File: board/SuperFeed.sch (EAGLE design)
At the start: 16 parts

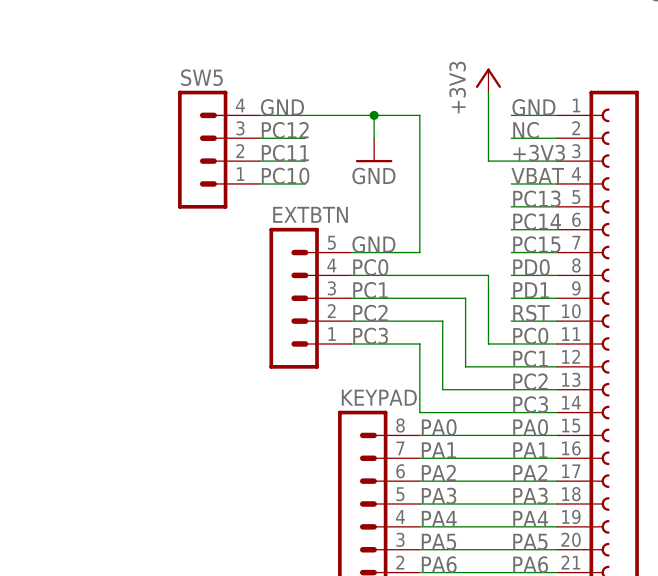
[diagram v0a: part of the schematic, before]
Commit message: Two more pins on extension connector
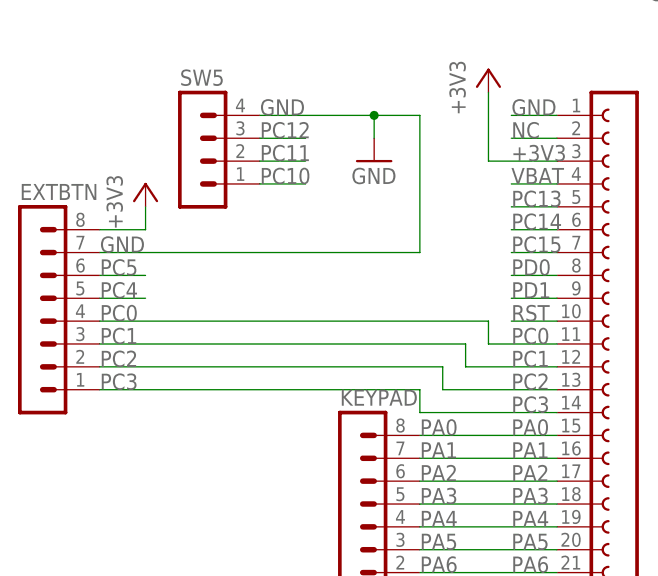
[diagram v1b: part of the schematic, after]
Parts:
- EXTBTN: device SuperFeed:MA05-1W -> SuperFeed:MA08-1W
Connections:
- net +3V3: now also EXTBTN.8
- net GND: now also EXTBTN.7; no longer EXTBTN.5
- net PC4: now also EXTBTN.5
- net PC5: now also EXTBTN.6
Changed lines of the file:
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@@
 <part name="R5" library="SuperFeed" deviceset="R-US_" device="0207/10" value="10k"/>
 <part name="P+5" library="SuperFeed" deviceset="+5V" device=""/>
-<part name="EXTBTN" library="SuperFeed" deviceset="MA05-1W" device=""/>
+<part name="EXTBTN" library="SuperFeed" deviceset="MA08-1W" device=""/>
+<part name="+3V3" library="SuperFeed" deviceset="+3V3" device=""/>
 </parts>
 <sheets>
@@
 <instance part="R5" gate="G$1" x="12.7" y="2.54"/>
 <instance part="P+5" gate="1" x="5.08" y="35.56"/>
-<instance part="EXTBTN" gate="G$1" x="12.7" y="76.2"/>
+<instance part="EXTBTN" gate="1" x="-15.24" y="73.66"/>
+<instance part="+3V3" gate="G$1" x="-2.54" y="88.9"/>
 </instances>
 <busses>
@@
 <wire x1="22.86" y1="96.52" x2="22.86" y2="93.98" width="0.1524" layer="91"/>
 <pinref part="GND5" gate="1" pin="GND"/>
-<pinref part="EXTBTN" gate="G$1" pin="5"/>
-<wire x1="20.32" y1="81.28" x2="27.94" y2="81.28" width="0.1524" layer="91"/>
-<wire x1="27.94" y1="81.28" x2="27.94" y2="96.52" width="0.1524" layer="91"/>
 <wire x1="27.94" y1="96.52" x2="22.86" y2="96.52" width="0.1524" layer="91"/>
 <junction x="22.86" y="96.52"/>
-<label x="20.32" y="81.28" size="1.778" layer="95"/>
+<pinref part="EXTBTN" gate="1" pin="7"/>
+<wire x1="-7.62" y1="81.28" x2="27.94" y2="81.28" width="0.1524" layer="91"/>
+<wire x1="27.94" y1="81.28" x2="27.94" y2="96.52" width="0.1524" layer="91"/>
+<label x="-7.62" y="81.28" size="1.778" layer="95"/>
 </segment>
 <segment>
@@
 <wire x1="96.52" y1="116.84" x2="88.9" y2="116.84" width="0.1524" layer="91"/>
 </segment>
+<segment>
+<pinref part="EXTBTN" gate="1" pin="8"/>
+<pinref part="+3V3" gate="G$1" pin="+3V3"/>
+<wire x1="-7.62" y1="83.82" x2="-2.54" y2="83.82" width="0.1524" layer="91"/>
+<wire x1="-2.54" y1="83.82" x2="-2.54" y2="86.36" width="0.1524" layer="91"/>
+</segment>
 </net>
 <net name="NC" class="0">
@@
 <segment>
 <pinref part="LEFT" gate="G$1" pin="23"/>
+<label x="38.1" y="40.64" size="1.778" layer="95"/>
 <wire x1="43.18" y1="40.64" x2="38.1" y2="40.64" width="0.1524" layer="91"/>
-<label x="38.1" y="40.64" size="1.778" layer="95"/>
+</segment>
+<segment>
+<pinref part="EXTBTN" gate="1" pin="5"/>
+<wire x1="-7.62" y1="76.2" x2="-2.54" y2="76.2" width="0.1524" layer="91"/>
+<label x="-7.62" y="76.2" size="1.778" layer="95"/>
 </segment>
 </net>
@@
 <segment>
 <pinref part="LEFT" gate="G$1" pin="24"/>
+<label x="38.1" y="38.1" size="1.778" layer="95"/>
 <wire x1="43.18" y1="38.1" x2="38.1" y2="38.1" width="0.1524" layer="91"/>
-<label x="38.1" y="38.1" size="1.778" layer="95"/>
+</segment>
+<segment>
+<pinref part="EXTBTN" gate="1" pin="6"/>
+<wire x1="-7.62" y1="78.74" x2="-2.54" y2="78.74" width="0.1524" layer="91"/>
+<label x="-7.62" y="78.74" size="1.778" layer="95"/>
 </segment>
 </net>
@@
 <label x="38.1" y="63.5" size="1.778" layer="95"/>
 <wire x1="43.18" y1="63.5" x2="27.94" y2="63.5" width="0.1524" layer="91"/>
-<wire x1="27.94" y1="63.5" x2="27.94" y2="71.12" width="0.1524" layer="91"/>
-<pinref part="EXTBTN" gate="G$1" pin="1"/>
-<wire x1="27.94" y1="71.12" x2="20.32" y2="71.12" width="0.1524" layer="91"/>
-<label x="20.32" y="71.12" size="1.778" layer="95"/>
+<wire x1="27.94" y1="63.5" x2="27.94" y2="66.04" width="0.1524" layer="91"/>
+<pinref part="EXTBTN" gate="1" pin="1"/>
+<wire x1="27.94" y1="66.04" x2="-7.62" y2="66.04" width="0.1524" layer="91"/>
+<label x="-7.62" y="66.04" size="1.778" layer="95"/>
 </segment>
 </net>
@@
 <label x="38.1" y="66.04" size="1.778" layer="95"/>
 <wire x1="43.18" y1="66.04" x2="30.48" y2="66.04" width="0.1524" layer="91"/>
-<wire x1="30.48" y1="66.04" x2="30.48" y2="73.66" width="0.1524" layer="91"/>
-<pinref part="EXTBTN" gate="G$1" pin="2"/>
-<wire x1="30.48" y1="73.66" x2="20.32" y2="73.66" width="0.1524" layer="91"/>
-<label x="20.32" y="73.66" size="1.778" layer="95"/>
+<wire x1="30.48" y1="66.04" x2="30.48" y2="68.58" width="0.1524" layer="91"/>
+<pinref part="EXTBTN" gate="1" pin="2"/>
+<wire x1="30.48" y1="68.58" x2="-7.62" y2="68.58" width="0.1524" layer="91"/>
+<label x="-7.62" y="68.58" size="1.778" layer="95"/>
 </segment>
 </net>
@@
 <label x="38.1" y="68.58" size="1.778" layer="95"/>
 <wire x1="43.18" y1="68.58" x2="33.02" y2="68.58" width="0.1524" layer="91"/>
-<wire x1="33.02" y1="68.58" x2="33.02" y2="76.2" width="0.1524" layer="91"/>
-<pinref part="EXTBTN" gate="G$1" pin="3"/>
-<wire x1="33.02" y1="76.2" x2="20.32" y2="76.2" width="0.1524" layer="91"/>
-<label x="20.32" y="76.2" size="1.778" layer="95"/>
+<wire x1="33.02" y1="68.58" x2="33.02" y2="71.12" width="0.1524" layer="91"/>
+<pinref part="EXTBTN" gate="1" pin="3"/>
+<wire x1="33.02" y1="71.12" x2="-7.62" y2="71.12" width="0.1524" layer="91"/>
+<label x="-7.62" y="71.12" size="1.778" layer="95"/>
 </segment>
 </net>
@@
 <wire x1="43.18" y1="71.12" x2="35.56" y2="71.12" width="0.1524" layer="91"/>
 <label x="38.1" y="71.12" size="1.778" layer="95"/>
-<wire x1="35.56" y1="71.12" x2="35.56" y2="78.74" width="0.1524" layer="91"/>
-<pinref part="EXTBTN" gate="G$1" pin="4"/>
-<wire x1="35.56" y1="78.74" x2="20.32" y2="78.74" width="0.1524" layer="91"/>
-<label x="20.32" y="78.74" size="1.778" layer="95"/>
-</segment>
-</net>
+<wire x1="35.56" y1="71.12" x2="35.56" y2="73.66" width="0.1524" layer="91"/>
+<pinref part="EXTBTN" gate="1" pin="4"/>
+<wire x1="35.56" y1="73.66" x2="-7.62" y2="73.66" width="0.1524" layer="91"/>
+<label x="-7.62" y="73.66" size="1.778" layer="95"/>
+</segment>
+</net>

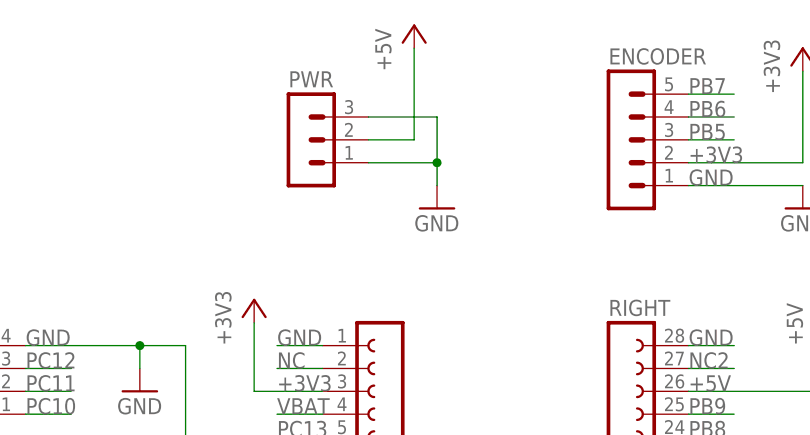
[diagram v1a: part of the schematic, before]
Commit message: Re-routing board to use GND plane on bottom side
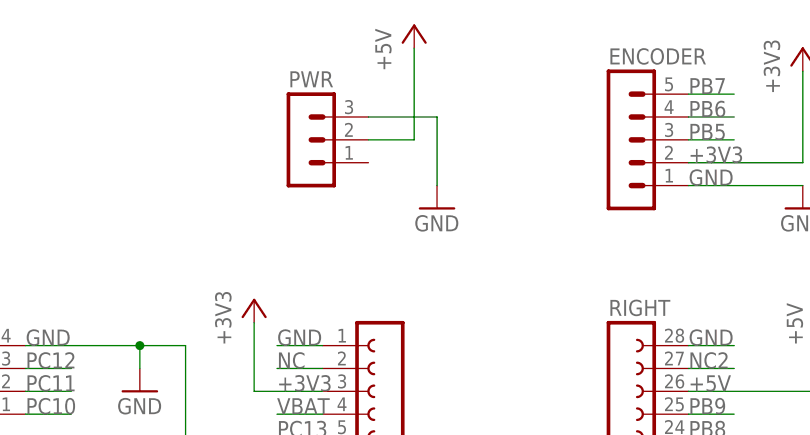
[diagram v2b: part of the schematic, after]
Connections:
- net GND: no longer PWR.1
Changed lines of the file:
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@@
 <pinref part="PWR" gate="G$1" pin="3"/>
 <wire x1="48.26" y1="121.92" x2="55.88" y2="121.92" width="0.1524" layer="91"/>
-<wire x1="55.88" y1="121.92" x2="55.88" y2="116.84" width="0.1524" layer="91"/>
+<wire x1="55.88" y1="121.92" x2="55.88" y2="114.3" width="0.1524" layer="91"/>
 <pinref part="GND4" gate="1" pin="GND"/>
-<pinref part="PWR" gate="G$1" pin="1"/>
-<wire x1="55.88" y1="116.84" x2="55.88" y2="114.3" width="0.1524" layer="91"/>
-<wire x1="48.26" y1="116.84" x2="55.88" y2="116.84" width="0.1524" layer="91"/>
-<junction x="55.88" y="116.84"/>
 </segment>
 <segment>

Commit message: Minor improvements to the board
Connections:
- net GND: now also PWR.1
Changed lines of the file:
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@@
 <pinref part="PWR" gate="G$1" pin="3"/>
 <wire x1="48.26" y1="121.92" x2="55.88" y2="121.92" width="0.1524" layer="91"/>
-<wire x1="55.88" y1="121.92" x2="55.88" y2="114.3" width="0.1524" layer="91"/>
+<wire x1="55.88" y1="121.92" x2="55.88" y2="116.84" width="0.1524" layer="91"/>
 <pinref part="GND4" gate="1" pin="GND"/>
+<pinref part="PWR" gate="G$1" pin="1"/>
+<wire x1="55.88" y1="116.84" x2="55.88" y2="114.3" width="0.1524" layer="91"/>
+<wire x1="48.26" y1="116.84" x2="55.88" y2="116.84" width="0.1524" layer="91"/>
+<junction x="55.88" y="116.84"/>
 </segment>
 <segment>
